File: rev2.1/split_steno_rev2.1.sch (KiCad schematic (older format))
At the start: 65 parts, among them J1 Audio-Jack-4, J2 USB_OTG, P1 TC2030-IDC, SW1 SW_Push, SW10 SW_Push, SW11 SW_Push, SW12 SW_Push, SW13 SW_Push, SW14 SW_Push, SW15 SW_Push, SW16 SW_Push, SW17 SW_Push, SW18 SW_Push, SW19 SW_Push, SW2 SW_Push, SW20 SW_Push, SW21 Switch-6P-2S2T, SW22 SW_Push, SW3 SW_Push, SW4 SW_Push, SW5 SW_Push, SW6 SW_Push, SW7 SW_Push, SW8 SW_Push, SW9 SW_Push, U1 74LVC1G34, U2 MCP73831, U3 MCP1700, U4 MCP1700, U5 ATXMEGA128A4U-AU, U6 nRF24L01_module

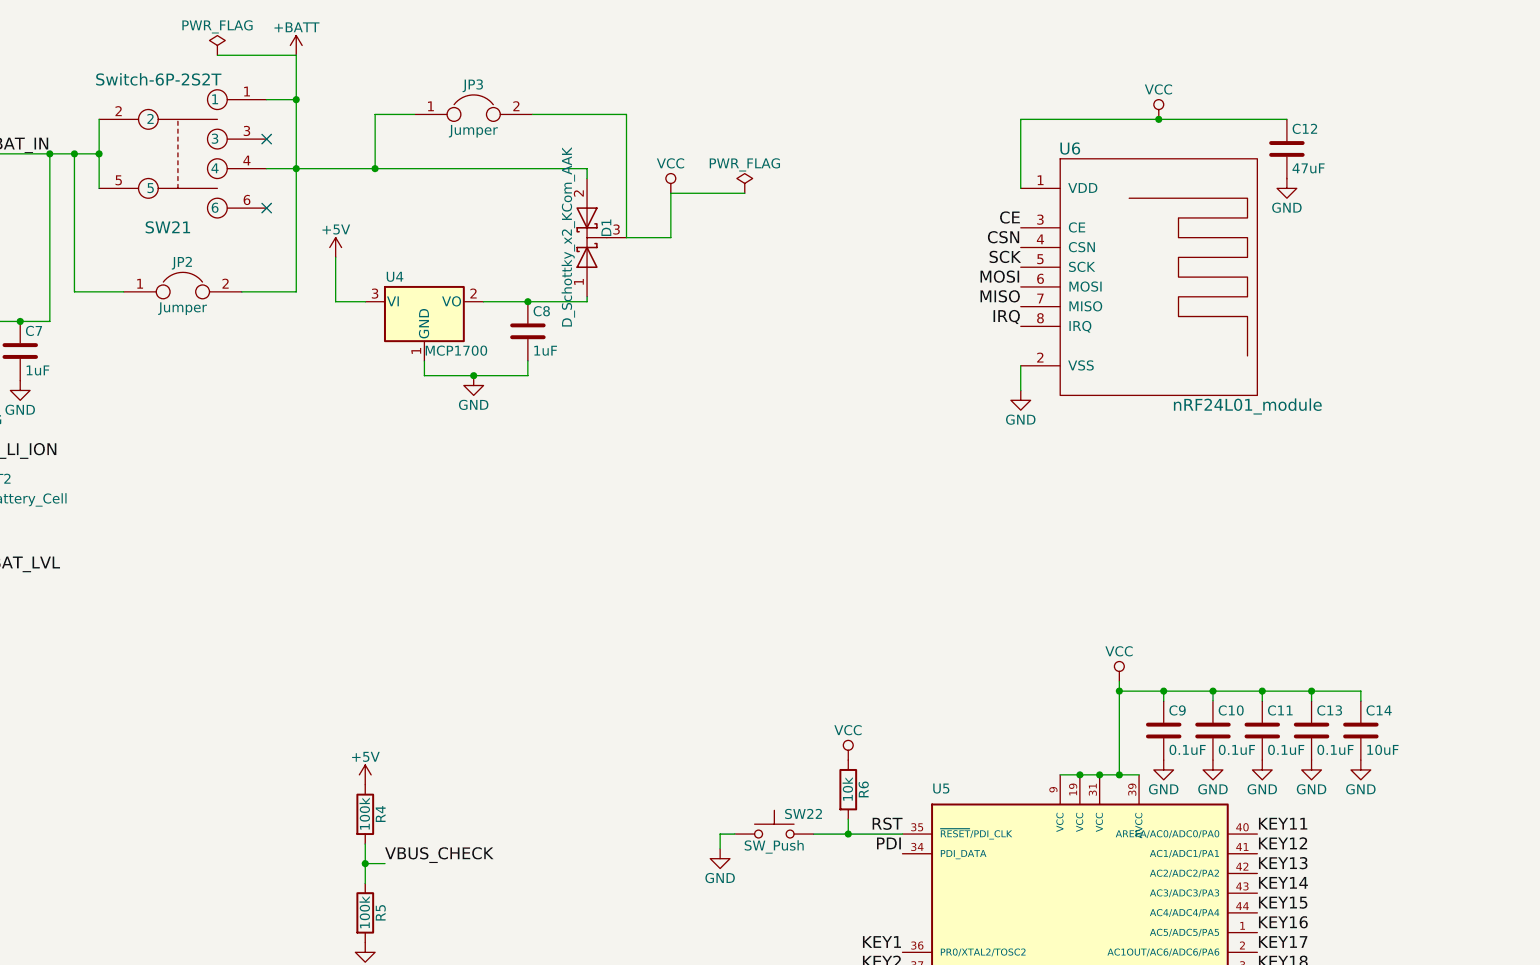
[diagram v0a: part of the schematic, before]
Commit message: split 2.0 into 2.1
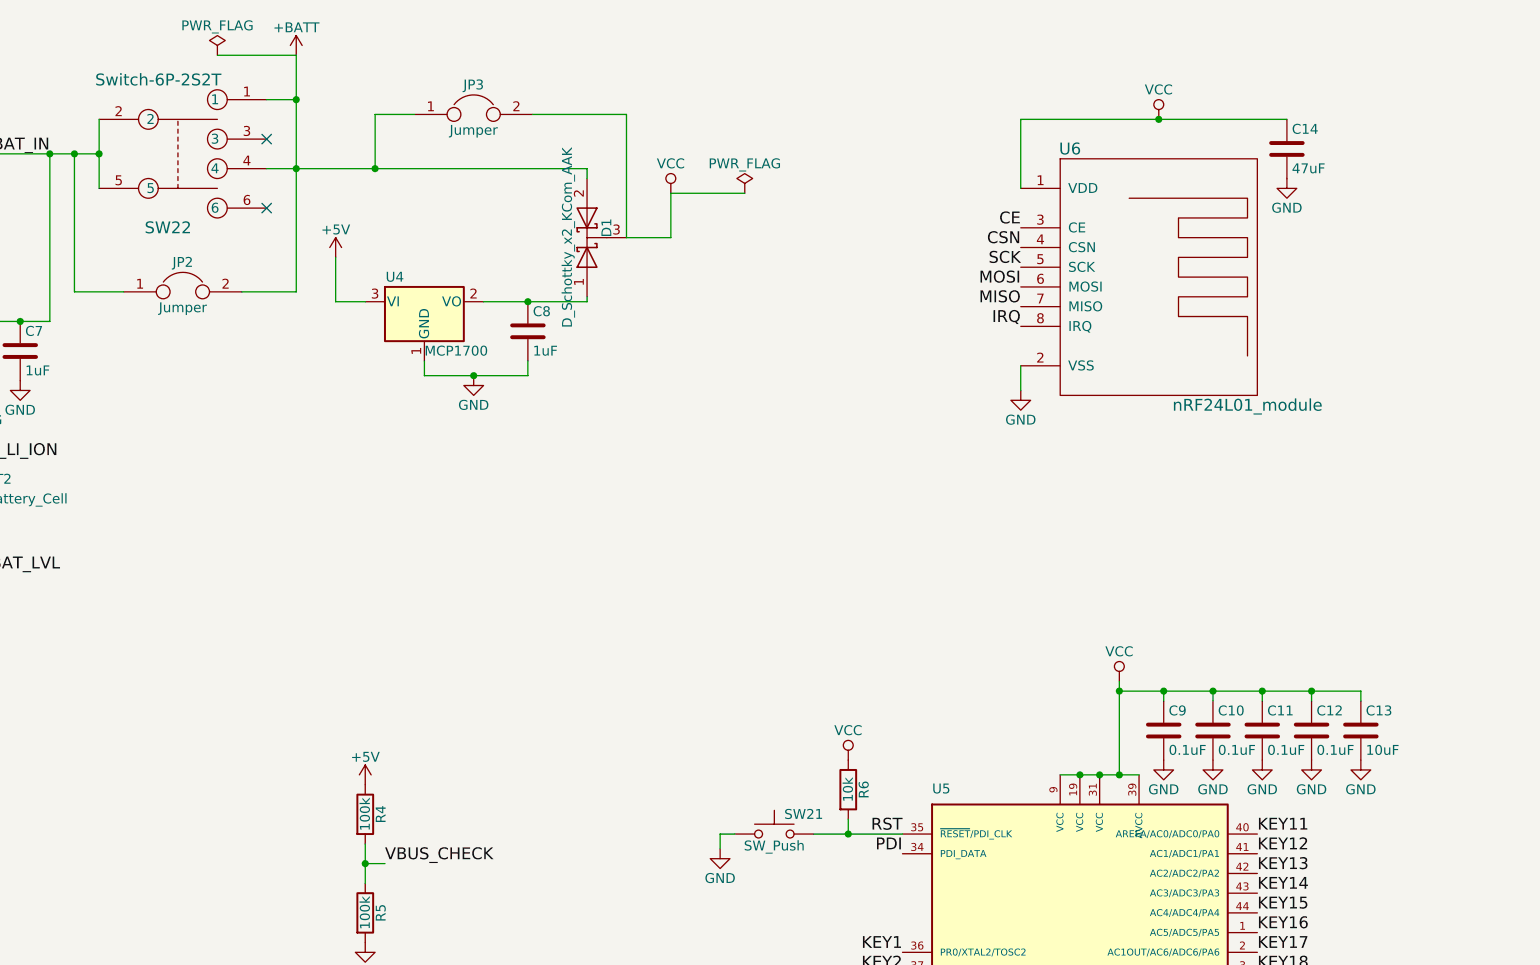
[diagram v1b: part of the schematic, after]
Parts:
- renumbered C13 to C12, C14 to C13, C12 to C14, SW22 to SW21, SW21 to SW22
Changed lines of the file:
@@
 LIBS:contrib
 LIBS:valves
-LIBS:split_steno_rev2.0-cache
+LIBS:split_steno_rev2.1-cache
 EELAYER 25 0
 EELAYER END
@@
 Sheet 1 1
 Title "split_steno"
-Date "2018-03-19"
-Rev "2.0"
+Date "2018-04-05"
+Rev "2.1"
 Comp "jtallbean"
 Comment1 ""
@@
 $EndComp
 $Comp
-L SW_Push SW22
+L SW_Push SW21
 U 1 1 5AB02100
 P 8425 4900
-F 0 "SW22" H 8475 5000 50  0000 L CNN
+F 0 "SW21" H 8475 5000 50  0000 L CNN
 F 1 "SW_Push" H 8425 4840 50  0000 C CNN
 F 2 "switch:SwitchPush_C&K_MultiFoot_RS-187R05A2-DS_And_PTS645_SMT" H 8425 5100 50  0001 C CNN
@@
 $EndComp
 $Comp
-L C C12
+L C C14
 U 1 1 5AB599DB
 P 11025 1425
-F 0 "C12" H 11050 1525 50  0000 L CNN
+F 0 "C14" H 11050 1525 50  0000 L CNN
 F 1 "47uF" H 11050 1325 50  0000 L CNN
 F 2 "Capacitors_SMD:C_0603_HandSoldering" H 11063 1275 50  0001 C CNN
@@
 $EndComp
 $Comp
-L C C13
+L C C12
 U 1 1 5AB555DB
 P 11150 4375
-F 0 "C13" H 11175 4475 50  0000 L CNN
+F 0 "C12" H 11175 4475 50  0000 L CNN
 F 1 "0.1uF" H 11175 4275 50  0000 L CNN
 F 2 "Capacitors_SMD:C_0603_HandSoldering" H 11188 4225 50  0001 C CNN
@@
 $EndComp
 $Comp
-L C C14
+L C C13
 U 1 1 5AB556F7
 P 11400 4375
-F 0 "C14" H 11425 4475 50  0000 L CNN
+F 0 "C13" H 11425 4475 50  0000 L CNN
 F 1 "10uF" H 11425 4275 50  0000 L CNN
 F 2 "Capacitors_SMD:C_0603_HandSoldering" H 11438 4225 50  0001 C CNN
@@
 $EndComp
 $Comp
-L Switch-6P-2S2T SW21
+L Switch-6P-2S2T SW22
 U 1 1 5AB5F6A2
 P 5350 1475
-F 0 "SW21" H 5350 1125 60  0000 C CNN
+F 0 "SW22" H 5350 1125 60  0000 C CNN
 F 1 "Switch-6P-2S2T" H 5300 1875 60  0000 C CNN
 F 2 "switch:SlideSwitch_C&K_JS202011CQN" H 5300 1675 60  0001 C CNN

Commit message: laid out pcb
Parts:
- removed R8: 100k, Resistors_SMD:R_0603_HandSoldering, symbol R
- SW13: footprint Keebio-Parts:Hybrid_PCB_100H_Dual_hole -> Keebio-Parts:Hybrid_PCB_100H_Dual_hole-flip
- renumbered C2 to C1, C3 to C2, C4 to C3, C5 to C4, C1 to C5, J2 to J1, J1 to J2, R9 to R8
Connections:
- net KEY13: now also U5.23 (PD3/OC0D/TXD0); no longer U5.42 (AC2/ADC2/PA2)
- net KEY8: now also U5.42 (AC2/ADC2/PA2); no longer U5.23 (PD3/OC0D/TXD0)
- no-connect marks 7 -> 8
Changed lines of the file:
@@
 $EndComp
 $Comp
-L Audio-Jack-4 J1
+L Audio-Jack-4 J2
 U 1 1 5AB02059
 P 14400 8475
-F 0 "J1" H 14350 8555 50  0000 C CNN
+F 0 "J2" H 14350 8555 50  0000 C CNN
 F 1 "Audio-Jack-4" H 14520 8105 50  0000 C CNN
 F 2 "Keebio-Parts:TRRS-PJ-320A" H 14650 8575 50  0001 C CNN
@@
 $EndComp
 $Comp
-L C C2
+L C C1
 U 1 1 5AB564A4
 P 2725 6325
-F 0 "C2" H 2750 6425 50  0000 L CNN
+F 0 "C1" H 2750 6425 50  0000 L CNN
 F 1 "0.1uF" H 2750 6225 50  0000 L CNN
 F 2 "Capacitors_SMD:C_0603_HandSoldering" H 2763 6175 50  0001 C CNN
@@
 $EndComp
 $Comp
-L C C3
+L C C2
 U 1 1 5AB56F27
 P 2725 7000
-F 0 "C3" H 2750 7100 50  0000 L CNN
+F 0 "C2" H 2750 7100 50  0000 L CNN
 F 1 "0.1uF" H 2750 6900 50  0000 L CNN
 F 2 "Capacitors_SMD:C_0603_HandSoldering" H 2763 6850 50  0001 C CNN
@@
 $EndComp
 $Comp
-L C C4
+L C C3
 U 1 1 5AB5704D
 P 3950 6325
-F 0 "C4" H 3975 6425 50  0000 L CNN
+F 0 "C3" H 3975 6425 50  0000 L CNN
 F 1 "0.1uF" H 3975 6225 50  0000 L CNN
 F 2 "Capacitors_SMD:C_0603_HandSoldering" H 3988 6175 50  0001 C CNN
@@
 $EndComp
 $Comp
-L C C5
+L C C4
 U 1 1 5AB572E0
 P 3950 7000
-F 0 "C5" H 3975 7100 50  0000 L CNN
+F 0 "C4" H 3975 7100 50  0000 L CNN
 F 1 "0.1uF" H 3975 6900 50  0000 L CNN
 F 2 "Capacitors_SMD:C_0603_HandSoldering" H 3988 6850 50  0001 C CNN
@@
 $EndComp
 $Comp
-L C C1
+L C C5
 U 1 1 5AB52BE0
 P 2250 3150
-F 0 "C1" H 2275 3250 50  0000 L CNN
+F 0 "C5" H 2275 3250 50  0000 L CNN
 F 1 "4.7uF" H 2275 3050 50  0000 L CNN
 F 2 "Capacitors_SMD:C_0603_HandSoldering" H 2288 3000 50  0001 C CNN
@@
 	1    0    0    -1
 $EndComp
-Text Label 6450 5050 0    60   ~ 0
-VBUS_CHECK
-$Comp
-L R R4
-U 1 1 5AB70EE7
-P 6350 4800
-F 0 "R4" V 6430 4800 50  0000 C CNN
-F 1 "100k" V 6350 4800 50  0000 C CNN
-F 2 "Resistors_SMD:R_0603_HandSoldering" V 6280 4800 50  0001 C CNN
-F 3 "" H 6350 4800 50  0001 C CNN
-	1    6350 4800
-	1    0    0    -1
-$EndComp
-$Comp
-L R R5
-U 1 1 5AB711AA
-P 6350 5300
-F 0 "R5" V 6430 5300 50  0000 C CNN
-F 1 "100k" V 6350 5300 50  0000 C CNN
-F 2 "Resistors_SMD:R_0603_HandSoldering" V 6280 5300 50  0001 C CNN
-F 3 "" H 6350 5300 50  0001 C CNN
-	1    6350 5300
-	1    0    0    -1
-$EndComp
-$Comp
-L +5V #PWR039
-U 1 1 5AB712BA
-P 6350 4650
-F 0 "#PWR039" H 6350 4500 50  0001 C CNN
-F 1 "+5V" H 6350 4790 50  0000 C CNN
-F 2 "" H 6350 4650 50  0001 C CNN
-F 3 "" H 6350 4650 50  0001 C CNN
-	1    6350 4650
-	1    0    0    -1
-$EndComp
-$Comp
-L GND #PWR040
-U 1 1 5AB7150E
-P 6350 5450
-F 0 "#PWR040" H 6350 5200 50  0001 C CNN
-F 1 "GND" H 6350 5300 50  0000 C CNN
-F 2 "" H 6350 5450 50  0001 C CNN
-F 3 "" H 6350 5450 50  0001 C CNN
-	1    6350 5450
-	1    0    0    -1
-$EndComp
 Text Label 10875 6300 0    60   ~ 0
 VBUS_CHECK
@@
 $EndComp
 $Comp
-L VCC #PWR041
+L VCC #PWR039
 U 1 1 5AB73ADB
 P 6775 6275
-F 0 "#PWR041" H 6775 6125 50  0001 C CNN
+F 0 "#PWR039" H 6775 6125 50  0001 C CNN
 F 1 "VCC" H 6775 6425 50  0000 C CNN
 F 2 "" H 6775 6275 50  0001 C CNN
@@
 $EndComp
 $Comp
-L GND #PWR042
+L GND #PWR040
 U 1 1 5AB73BB1
 P 6775 6775
-F 0 "#PWR042" H 6775 6525 50  0001 C CNN
+F 0 "#PWR040" H 6775 6525 50  0001 C CNN
 F 1 "GND" H 6775 6625 50  0000 C CNN
 F 2 "" H 6775 6775 50  0001 C CNN
@@
 	7675 1250 7675 1875
 Wire Wire Line
-	6350 4950 6350 5150
-Wire Wire Line
-	6450 5050 6350 5050
-Connection ~ 6350 5050
-Wire Wire Line
 	6775 6425 6775 6275
 Wire Wire Line
 	6775 6625 6775 6775
 $Comp
-L Fuse F1
-U 1 1 5AB75E08
-P 14025 6700
-F 0 "F1" V 14105 6700 50  0000 C CNN
-F 1 "Fuse" V 13950 6700 50  0000 C CNN
-F 2 "Fuse_Holders_and_Fuses:Fuse_SMD1206_HandSoldering" V 13955 6700 50  0001 C CNN
-F 3 "" H 14025 6700 50  0001 C CNN
-	1    14025 6700
-	0    1    1    0
-$EndComp
-$Comp
-L +5V #PWR043
+L +5V #PWR041
 U 1 1 5AB75F33
 P 13875 6700
-F 0 "#PWR043" H 13875 6550 50  0001 C CNN
+F 0 "#PWR041" H 13875 6550 50  0001 C CNN
 F 1 "+5V" H 13875 6840 50  0000 C CNN
 F 2 "" H 13875 6700 50  0001 C CNN
@@
 	1    13875 6700
 	0    -1   -1   0
-$EndComp
-$Comp
-L R R8
-U 1 1 5AB761AA
-P 14025 7100
-F 0 "R8" V 14105 7100 50  0000 C CNN
-F 1 "100k" V 14025 7100 50  0000 C CNN
-F 2 "Resistors_SMD:R_0603_HandSoldering" V 13955 7100 50  0001 C CNN
-F 3 "" H 14025 7100 50  0001 C CNN
-	1    14025 7100
-	0    1    1    0
-$EndComp
-$Comp
-L GND #PWR044
-U 1 1 5AB7667C
-P 13875 7100
-F 0 "#PWR044" H 13875 6850 50  0001 C CNN
-F 1 "GND" H 13875 6950 50  0000 C CNN
-F 2 "" H 13875 7100 50  0001 C CNN
-F 3 "" H 13875 7100 50  0001 C CNN
-	1    13875 7100
-	0    1    1    0
 $EndComp
 Text Label 14175 7000 2    60   ~ 0
@@
 F 0 "SW13" H 4525 9100 50  0000 L CNN
 F 1 "SW_Push" H 4475 8940 50  0000 C CNN
-F 2 "Keebio-Parts:Hybrid_PCB_100H_Dual_hole" H 4475 9200 50  0001 C CNN
+F 2 "Keebio-Parts:Hybrid_PCB_100H_Dual_hole-flip" H 4475 9200 50  0001 C CNN
 F 3 "" H 4475 9200 50  0001 C CNN
 	1    4475 9000
@@
 KEY18
 $Comp
-L GND #PWR045
+L GND #PWR042
 U 1 1 5ABA1B58
 P 5400 9950
-F 0 "#PWR045" H 5400 9700 50  0001 C CNN
+F 0 "#PWR042" H 5400 9700 50  0001 C CNN
 F 1 "GND" H 5400 9800 50  0000 C CNN
 F 2 "" H 5400 9950 50  0001 C CNN
@@
 $EndComp
 $Comp
-L GND #PWR046
+L GND #PWR043
 U 1 1 5ABA1C2A
 P 4675 9950
-F 0 "#PWR046" H 4675 9700 50  0001 C CNN
+F 0 "#PWR043" H 4675 9700 50  0001 C CNN
 F 1 "GND" H 4675 9800 50  0000 C CNN
 F 2 "" H 4675 9950 50  0001 C CNN
@@
 $EndComp
 $Comp
-L GND #PWR047
+L GND #PWR044
 U 1 1 5ABA1DBF
 P 3950 9950
-F 0 "#PWR047" H 3950 9700 50  0001 C CNN
+F 0 "#PWR044" H 3950 9700 50  0001 C CNN
 F 1 "GND" H 3950 9800 50  0000 C CNN
 F 2 "" H 3950 9950 50  0001 C CNN
@@
 $EndComp
 $Comp
-L GND #PWR048
+L GND #PWR045
 U 1 1 5ABA1E8A
 P 3225 9950
-F 0 "#PWR048" H 3225 9700 50  0001 C CNN
+F 0 "#PWR045" H 3225 9700 50  0001 C CNN
 F 1 "GND" H 3225 9800 50  0000 C CNN
 F 2 "" H 3225 9950 50  0001 C CNN
@@
 $EndComp
 $Comp
-L GND #PWR049
+L GND #PWR046
 U 1 1 5ABA1F55
 P 2500 9950
-F 0 "#PWR049" H 2500 9700 50  0001 C CNN
+F 0 "#PWR046" H 2500 9700 50  0001 C CNN
 F 1 "GND" H 2500 9800 50  0000 C CNN
 F 2 "" H 2500 9950 50  0001 C CNN
@@
 Connection ~ 5400 9750
 $Comp
-L USB_OTG J2
+L USB_OTG J1
 U 1 1 5ABA2F3D
 P 14475 6900
-F 0 "J2" H 14275 7350 50  0000 L CNN
+F 0 "J1" H 14275 7350 50  0000 L CNN
 F 1 "USB_OTG" H 14275 7250 50  0000 L CNN
 F 2 "keyboard_parts:USB_miniB" H 14625 6850 50  0001 C CNN
@@
 NoConn ~ 14575 7300
 $Comp
-L GND #PWR050
+L GND #PWR047
 U 1 1 5ABA70EC
 P 14475 7300
-F 0 "#PWR050" H 14475 7050 50  0001 C CNN
+F 0 "#PWR047" H 14475 7050 50  0001 C CNN
 F 1 "GND" H 14475 7150 50  0000 C CNN
 F 2 "" H 14475 7300 50  0001 C CNN
@@
 $EndComp
 $Comp
-L GND #PWR051
+L GND #PWR048
 U 1 1 5ABAC1AF
 P 14600 8875
-F 0 "#PWR051" H 14600 8625 50  0001 C CNN
+F 0 "#PWR048" H 14600 8625 50  0001 C CNN
 F 1 "GND" H 14600 8725 50  0000 C CNN
 F 2 "" H 14600 8875 50  0001 C CNN
@@
 SCL
 $Comp
-L +3.3V #PWR052
+L +3.3V #PWR049
 U 1 1 5ABB66D1
 P 13950 8875
-F 0 "#PWR052" H 13950 8725 50  0001 C CNN
+F 0 "#PWR049" H 13950 8725 50  0001 C CNN
 F 1 "+3.3V" H 13950 9015 50  0000 C CNN
 F 2 "" H 13950 8875 50  0001 C CNN
@@
 	13950 8675 13950 8875
 $Comp
-L R R9
+L R R8
 U 1 1 5ABB72D4
 P 14050 8425
-F 0 "R9" V 14130 8425 50  0000 C CNN
+F 0 "R8" V 14130 8425 50  0000 C CNN
 F 1 "4.7k" V 14050 8425 50  0000 C CNN
 F 2 "Resistors_SMD:R_0603_HandSoldering" V 13980 8425 50  0001 C CNN
@@
 Connection ~ 14050 8575
 $Comp
-L +3.3V #PWR053
+L +3.3V #PWR050
 U 1 1 5ABB8032
 P 14050 8275
-F 0 "#PWR053" H 14050 8125 50  0001 C CNN
+F 0 "#PWR050" H 14050 8125 50  0001 C CNN
 F 1 "+3.3V" H 14050 8415 50  0000 C CNN
 F 2 "" H 14050 8275 50  0001 C CNN
@@
 $EndComp
 $Comp
-L +3.3V #PWR054
+L +3.3V #PWR051
 U 1 1 5ABB820B
 P 13875 8175
-F 0 "#PWR054" H 13875 8025 50  0001 C CNN
+F 0 "#PWR051" H 13875 8025 50  0001 C CNN
 F 1 "+3.3V" H 13875 8315 50  0000 C CNN
 F 2 "" H 13875 8175 50  0001 C CNN
@@
 Text Label 9075 6400 2    60   ~ 0
 KEY7
-Text Label 9075 6500 2    60   ~ 0
+Text Label 10875 5100 0    60   ~ 0
 KEY8
 Text Label 9075 6600 2    60   ~ 0
@@
 Text Label 10875 5000 0    60   ~ 0
 KEY12
-Text Label 10875 5100 0    60   ~ 0
+Text Label 9075 6500 2    60   ~ 0
 KEY13
 Text Label 10875 5200 0    60   ~ 0
@@
 KEY18
 NoConn ~ 10875 5750
+$Comp
+L Fuse F1
+U 1 1 5AB75E08
+P 14025 6700
+F 0 "F1" V 14105 6700 50  0000 C CNN
+F 1 "Fuse" V 13950 6700 50  0000 C CNN
+F 2 "Fuse_Holders_and_Fuses:Fuse_SMD1206_HandSoldering" V 13955 6700 50  0001 C CNN
+F 3 "" H 14025 6700 50  0001 C CNN
+	1    14025 6700
+	0    1    1    0
+$EndComp
+Connection ~ 6350 5050
+Wire Wire Line
+	6450 5050 6350 5050
+Wire Wire Line
+	6350 4950 6350 5150
+$Comp
+L GND #PWR052
+U 1 1 5AB7150E
+P 6350 5450
+F 0 "#PWR052" H 6350 5200 50  0001 C CNN
+F 1 "GND" H 6350 5300 50  0000 C CNN
+F 2 "" H 6350 5450 50  0001 C CNN
+F 3 "" H 6350 5450 50  0001 C CNN
+	1    6350 5450
+	1    0    0    -1
+$EndComp
+$Comp
+L +5V #PWR053
+U 1 1 5AB712BA
+P 6350 4650
+F 0 "#PWR053" H 6350 4500 50  0001 C CNN
+F 1 "+5V" H 6350 4790 50  0000 C CNN
+F 2 "" H 6350 4650 50  0001 C CNN
+F 3 "" H 6350 4650 50  0001 C CNN
+	1    6350 4650
+	1    0    0    -1
+$EndComp
+$Comp
+L R R5
+U 1 1 5AB711AA
+P 6350 5300
+F 0 "R5" V 6430 5300 50  0000 C CNN
+F 1 "100k" V 6350 5300 50  0000 C CNN
+F 2 "Resistors_SMD:R_0603_HandSoldering" V 6280 5300 50  0001 C CNN
+F 3 "" H 6350 5300 50  0001 C CNN
+	1    6350 5300
+	1    0    0    -1
+$EndComp
+$Comp
+L R R4
+U 1 1 5AB70EE7
+P 6350 4800
+F 0 "R4" V 6430 4800 50  0000 C CNN
+F 1 "100k" V 6350 4800 50  0000 C CNN
+F 2 "Resistors_SMD:R_0603_HandSoldering" V 6280 4800 50  0001 C CNN
+F 3 "" H 6350 4800 50  0001 C CNN
+	1    6350 4800
+	1    0    0    -1
+$EndComp
+Text Label 6450 5050 0    60   ~ 0
+VBUS_CHECK
+NoConn ~ 14175 7100
 $EndSCHEMATC
